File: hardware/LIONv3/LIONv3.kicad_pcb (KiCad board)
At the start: 4 copper layers, 45 x 80 mm, 77 parts, among them SW1 RESET, SW2 BOOT, U1 TCAN3414DR, U10 INA226AIDGSR, U11 TPS259474ARPWR, U12 XL-1608UGC-04, U13 XL-1608SURC-06, U14 UART, U15 I2C, U16 CAN, U17 PWR_3V3, U18 PWR_5V, U19 PWR_GND, U2 TYPE-C_16PIN_2MD(073), U20 TLV76733DRVR, U3 ESP32-C6-MINI-1-N4, U4 TMP112AIDRLR, U5 E80-900M2213S, U6 INA226AIDGSR, U7 XL-1608UBC-04, U8 W25Q16JVSSIQTR

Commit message: feat(hardware): add final components position
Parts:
- added H1: M2.5, MountingHole:MountingHole_2.5mm_Pad_Via, F.Cu at (2.77, 2.77)
- added H2: M2.5, MountingHole:MountingHole_2.5mm_Pad_Via, F.Cu at (2.77, 9.32)
- added H3: M2.5, MountingHole:MountingHole_2.5mm_Pad_Via, F.Cu at (2.77, 15.9)
- added H4: M2.5, MountingHole:MountingHole_2.5mm_Pad_Via, F.Cu at (2.77, 22.4)
- added U9: HC-1_25-2PWT, LIONv3-Footprints:CONN-SMD_2P-P1.25-HC-1.25-2PWT, B.Cu at (199.7, 75.2)
- C16, C17, C18, C19, C20, C21, C22, D3, D4, R17, R18, R19, R20, R21, R22, R23, R32, U10, U11, U20: moved to B.Cu
- U14: value UART -> HC-1_25-2PWT; footprint LIONv3-Footprints:CONN-SMD_4P-P1.25_53261-0471 -> LIONv3-Footprints:CONN-SMD_2P-P1.25-HC-1.25-2PWT
- U15: value I2C -> HC-1_25-2PWT; footprint LIONv3-Footprints:CONN-SMD_4P-P1.25_53261-0471 -> LIONv3-Footprints:CONN-SMD_2P-P1.25-HC-1.25-2PWT
- U16: value CAN -> HC-1_25-2PWT; footprint LIONv3-Footprints:CONN-SMD_4P-P1.25_53261-0471 -> LIONv3-Footprints:CONN-SMD_2P-P1.25-HC-1.25-2PWT
- U17: value PWR_3V3 -> HC-1_25-2PWT; footprint LIONv3-Footprints:CONN-SMD_4P-P1.25_53261-0471 -> LIONv3-Footprints:CONN-SMD_2P-P1.25-HC-1.25-2PWT
- U18: value PWR_5V -> HC-1_25-2PWT; footprint LIONv3-Footprints:CONN-SMD_4P-P1.25_53261-0471 -> LIONv3-Footprints:CONN-SMD_2P-P1.25-HC-1.25-2PWT
- U19: value PWR_GND -> HC-1_25-2PWT; footprint LIONv3-Footprints:CONN-SMD_4P-P1.25_53261-0471 -> LIONv3-Footprints:CONN-SMD_2P-P1.25-HC-1.25-2PWT
- moved U17 122.7 mm to (199.2, 84.6), turned to -90 degrees
- moved U16 114.2 mm to (199.2, 94.3), turned to -90 degrees
- moved U14 94.1 mm to (162.1, 85.5), turned to 90 degrees
- moved U15 88.1 mm to (162.1, 76.9), turned to 90 degrees
- moved R12 88.0 mm to (184.1, 95.3)
- moved U6 88.0 mm to (178.2, 96.1)
- moved C12 88.0 mm to (182.1, 96.8)
- moved D1 85.6 mm to (168.1, 85.5), turned to 0 degrees
- moved U18 83.9 mm to (162.1, 68.3), turned to 90 degrees
- moved R18 79.9 mm to (186.4, 70.8), turned to 180 degrees
- moved C16 79.6 mm to (184.9, 72.5), turned to 0 degrees
- moved JP1 77.9 mm to (170.4, 82.4), turned to 90 degrees
- moved R3 76.0 mm to (169.7, 88.4), turned to 90 degrees
- moved U10 74.4 mm to (185.7, 76.3), turned to 180 degrees
- moved R2 74.4 mm to (170.9, 88.4), turned to -90 degrees
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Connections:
- D1 pad 1: /CAN_A_P -> /CAN_A_N
- D1 pad 2: /CAN_A_N -> /CAN_A_P
- U14 pad 1: +3.3V -> /CAN_A_N
- U14 pad 2: /UART_TX0 -> /CAN_A_P
- U14 pad 3: /UART_RX0 -> GND
- U15 pad 1: /I2C_SDA -> /I2C_SCL
- U15 pad 2: unconnected-(U15-Pad2) -> /I2C_SDA
- U15 pad 3: unconnected-(U15-Pad3) -> GND
- U15 pad 4: /I2C_SCL -> GND
- U16 pad 1: unconnected-(U16-Pad1) -> /3V3_IN
- U16 pad 2: /CAN_A_P -> /3V3_IN
- U16 pad 3: /CAN_A_N -> GND
- U16 pad 4: unconnected-(U16-Pad4) -> GND
- U17 pad 1: /3V3_IN -> +5V
- U17 pad 2: /3V3_IN -> +5V
- U17 pad 3: /3V3_IN -> GND
- U17 pad 4: /3V3_IN -> GND
- U18 pad 1: +5V -> GND
- U18 pad 2: +5V -> GND
- U18 pad 3: +5V -> GND
- U18 pad 4: +5V -> GND
- U19 pad 1: GND -> /CAN_A_N
- U19 pad 2: GND -> /CAN_A_P
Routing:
- net +3.3V: vias 21 -> 1
- net GND: vias 20 -> 69
- net /POWER/PWR: vias 13 -> 2
- net /POWER/5V_D: vias 8 -> 2
- net /POWER/3V3_IN: vias 19 -> 0
- added copper zone on B.Cu, net /POWER/5V_D
- added copper zone on B.Cu, net /POWER/PWR
- added copper zone on B.Cu, net GND
- removed copper zone on F.Cu, net +3.3V
- removed copper zone on F.Cu, net /POWER/3V3_IN
- removed copper zone on F.Cu, net /POWER/5V_D
- removed copper zone on F.Cu, net /POWER/PWR
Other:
- board size 45 x 80 mm -> 45 x 85.1 mm

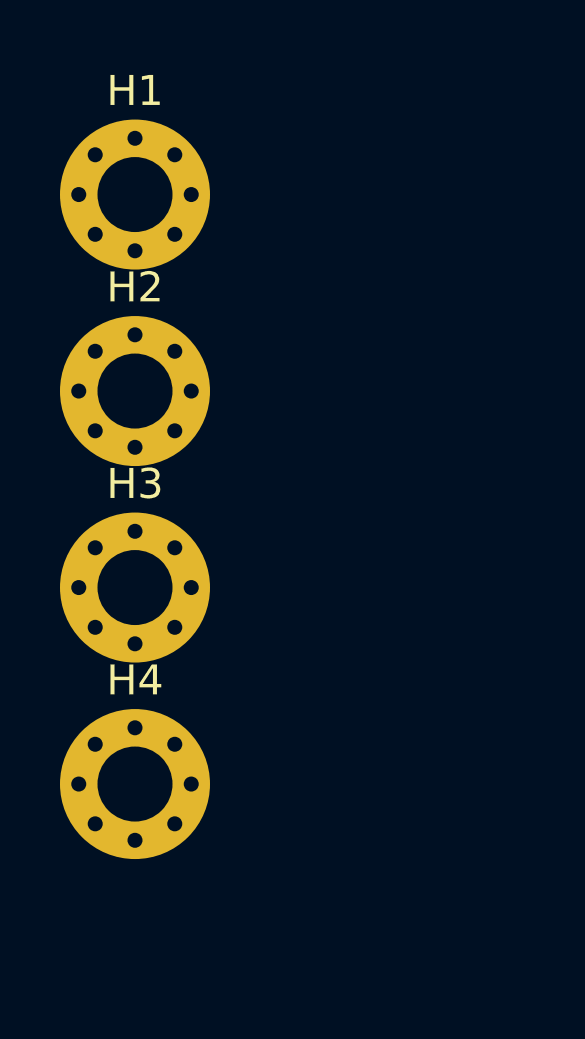
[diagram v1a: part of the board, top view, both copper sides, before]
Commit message: feat(hardware): organize repo structure
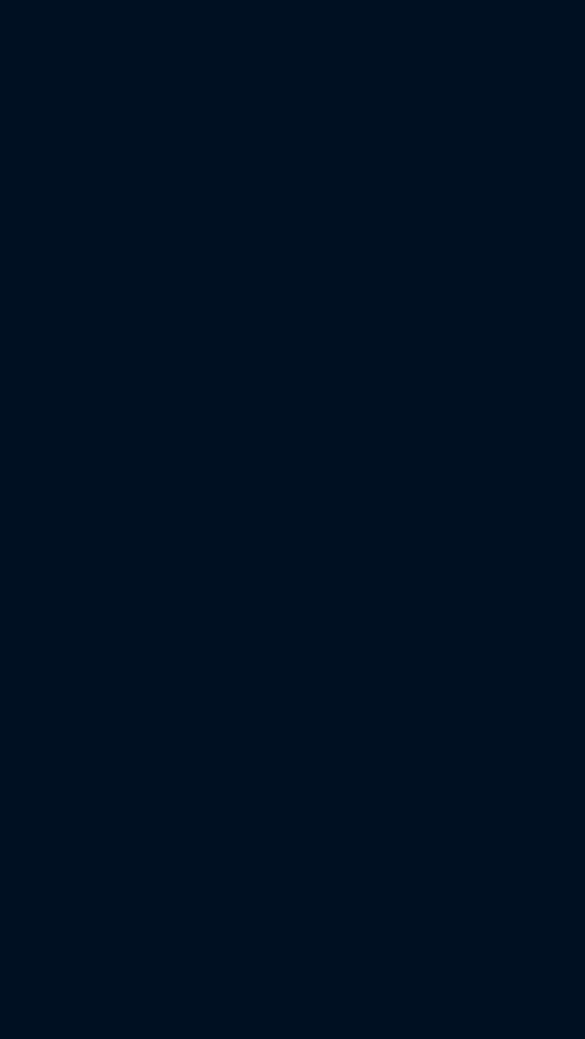
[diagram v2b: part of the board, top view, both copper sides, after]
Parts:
- removed H1, H2, H3, H4: M2.5, MountingHole:MountingHole_2.5mm_Pad_Via

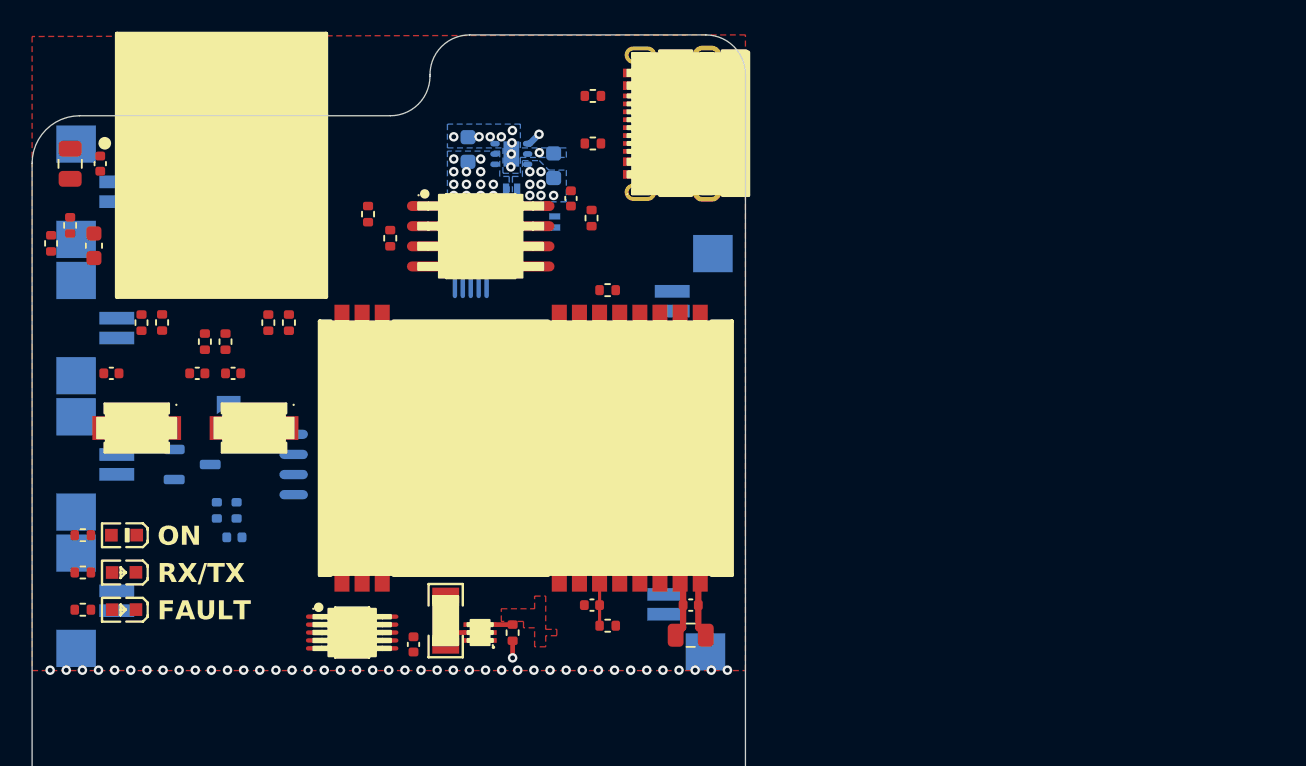
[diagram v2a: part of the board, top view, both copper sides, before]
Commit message: feat(hardware): add power layout
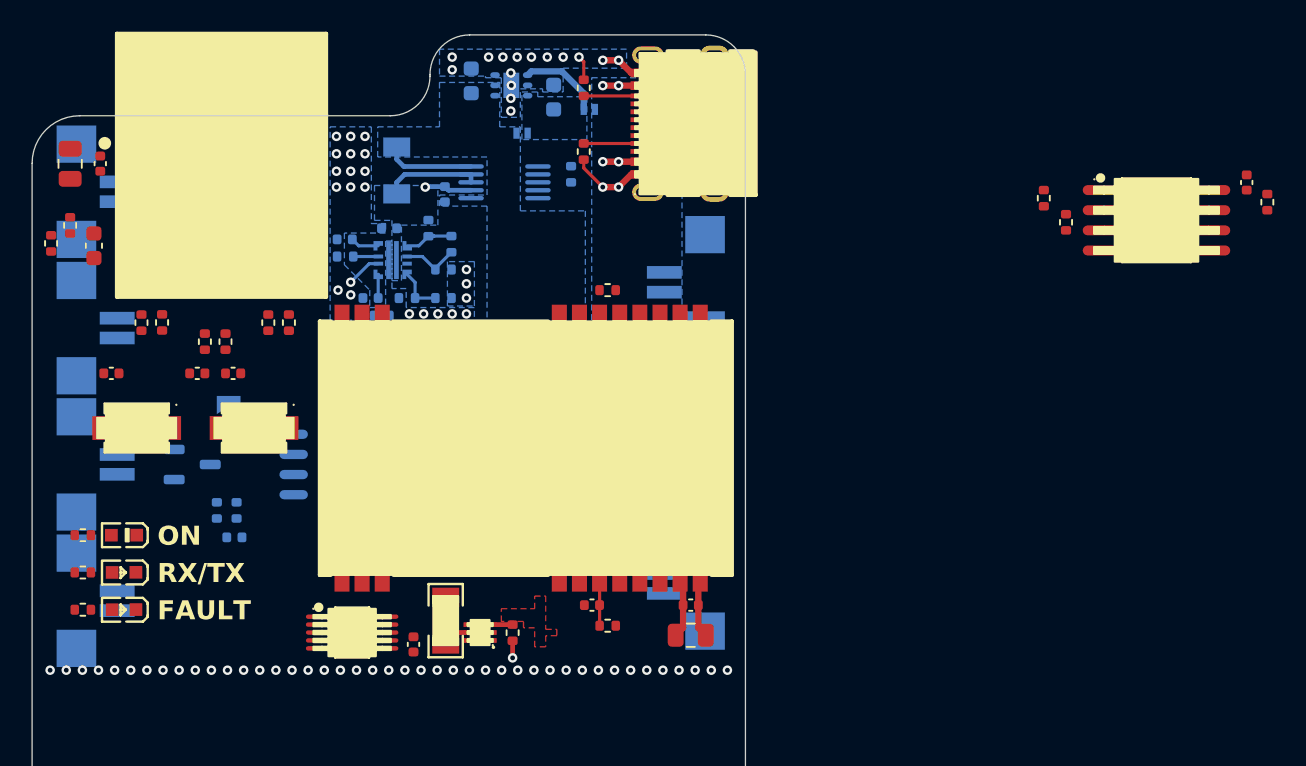
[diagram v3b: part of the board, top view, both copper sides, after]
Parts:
- moved C13 42.6 mm to (234.6, 67.7)
- moved R13 42.6 mm to (221.8, 68.7)
- moved R16 42.6 mm to (223.2, 70.2)
- moved U8 42.6 mm to (228.9, 70.1)
- moved R15 42.6 mm to (235.9, 68.9)
- moved U9 17.8 mm to (199.2, 93.0)
- moved R19 16.9 mm to (183.0, 70.6)
- moved R20 16.7 mm to (184.4, 71.6)
- moved C20 16.7 mm to (180.1, 76.1)
- moved R21 16.7 mm to (177.8, 72.4)
- moved R23 16.7 mm to (183.9, 75.0)
- moved R32 16.7 mm to (183.9, 73.2)
- moved C18 16.7 mm to (177.7, 71.3)
- moved C19 16.7 mm to (179.3, 75.0)
- moved R22 16.7 mm to (181.7, 75.0)
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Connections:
- U16 pad 1: /3V3_IN -> /POWER/PWR
- U16 pad 2: /3V3_IN -> /POWER/PWR
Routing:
- net GND: track 6.22 -> 24.3 mm, vias 69 -> 82
- net /POWER/3V3_IN: track 0.00 -> 6.13 mm
- net /POWER/PWR: track 0.00 -> 5.66 mm, vias 2 -> 0
- net +5V: track 0.00 -> 4.60 mm, vias 0 -> 4
- net /POWER/5V_D: track 0.97 -> 5.22 mm, vias 2 -> 0
- net Net-(U2-CC2): track 0.00 -> 3.50 mm
- net Net-(U2-CC1): track 0.00 -> 3.50 mm
- net +3.3V: vias 1 -> 11
- added copper zone on B.Cu, net +3.3V
- added copper zone on In2.Cu, net +3.3V
- added copper zone on B.Cu, net +5V
- added copper zone on B.Cu, net /POWER/3V3_IN
- added copper zone on In1.Cu, net GND

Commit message: feat(hardware): add RF circuit
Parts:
- removed U19: HC-1_25-2PWT, LIONv3-Footprints:CONN-SMD_2P-P1.25-HC-1.25-2PWT
- C12, R12, U6: moved to B.Cu
- moved R15 18.5 mm to (218.2, 63.9), turned to 0 degrees
- moved C13 17.9 mm to (216.9, 65.2), turned to 180 degrees
- moved R12 14.9 mm to (176.8, 82.3)
- moved U6 13.8 mm to (182.7, 83.1)
- moved C12 13.4 mm to (178.8, 83.8)
- moved U18 12.4 mm to (150.0, 65.4)
- moved R13 10.1 mm to (217.9, 78.0), turned to 180 degrees
- moved U8 9.66 mm to (219.3, 70.9), turned to 0 degrees
- moved R16 7.43 mm to (219.4, 76.6), turned to 0 degrees
- moved C1 7.00 mm to (183.4, 92.5)
- moved C2 7.00 mm to (181.6, 92.5)
- moved C6 7.00 mm to (170.8, 97.1)
- moved D1 7.00 mm to (168.1, 92.5)
- moved JP1 7.00 mm to (170.4, 89.4)
- moved R2 7.00 mm to (170.9, 95.4)
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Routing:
- net Net-(C3-Pad1): track 0.00 -> 12.6 mm
- net GND: track 24.3 -> 36.8 mm, vias 82 -> 124
- net +3.3V: track 2.28 -> 14.7 mm, vias 11 -> 15
- net /IO9: track 0.00 -> 9.00 mm, vias 0 -> 2
- net /I2C_SDA: track 0.00 -> 7.00 mm, vias 0 -> 1
- net /I2C_SCL: track 0.00 -> 6.96 mm, vias 0 -> 1
- net Net-(U3-EN): track 0.00 -> 4.85 mm
- net 3.3V_RF: track 4.07 -> 8.36 mm, vias 0 -> 2
- net /LR_NSS: track 0.00 -> 3.48 mm, vias 0 -> 1
- net /IO8: track 0.00 -> 1.80 mm
- net /TMP_ALERT: track 1.30 -> 2.36 mm, vias 0 -> 1
- net /LR_RST: track 3.20 -> 4.00 mm

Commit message: feat(hardware): change SPI terminology (new OSHWA naming conventions)
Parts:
- removed C3: 100nF, Capacitor_SMD:C_0402_1005Metric
- removed R1: 0, Resistor_SMD:R_0402_1005Metric
- added C23: 100nF, Capacitor_SMD:C_0402_1005Metric, F.Cu at (245.4, 100.3)
- added D2: ESD9B3.3ST5G, Diode_SMD:D_SOD-923, F.Cu at (252.8, 102.7)
- added D5: ESD9B3.3ST5G, Diode_SMD:D_SOD-923, F.Cu at (248.2, 105.9)
- added D6: D_Schottky, LIONv3-Footprints:X2-DFN1006-2_L1.0-W0.6-P0.65-RD, F.Cu at (251.6, 92.8)
- added FB1: 220Ω@100MHz, Capacitor_SMD:C_0805_2012Metric, F.Cu at (259.2, 105.5)
- added FB2: 220Ω@100MHz, Capacitor_SMD:C_0805_2012Metric, F.Cu at (239.1, 108.3)
- added U19: HC-1_25-2PWT, LIONv3-Footprints:CONN-SMD_2P-P1.25-HC-1.25-2PWT, F.Cu at (235.0, 93.6)
- added U21: USBLC6-2SC6, Package_TO_SOT_SMD:SOT-23-6, F.Cu at (226.9, 100.5)
- R14: value 68 -> 1k
- R24: value 82 -> 2.2k
- R25: value 150 -> 1k
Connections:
- C21 pad 1: /POWER/5V_D -> +5V
- C4 pad 1: Net-(U3-EN) -> Net-(D2-A2)
- D3 pad 1: /POWER/5V_D -> +5V
- D3 pad 2: +5V -> Net-(D3-A)
- D4 pad 1: /POWER/5V_D -> +5V
- R4 pad 2: Net-(U3-EN) -> Net-(D2-A2)
- SW1 pad 2: Net-(C3-Pad1) -> Net-(D2-A2)
- U17 pad 1: +5V -> Net-(FB2-Pad2)
- U17 pad 2: +5V -> Net-(FB2-Pad2)
- U2 pad A4B9: +5V -> Net-(FB1-Pad2)
- U2 pad A6: /USB_D+ -> /D+
- U2 pad A7: /USB_D- -> /D-
- U2 pad B4A9: +5V -> Net-(FB1-Pad2)
- U2 pad B6: /USB_D+ -> /D+
- U2 pad B7: /USB_D- -> /D-
- U20 pad 4: /POWER/5V_D -> +5V
- U20 pad 6: /POWER/5V_D -> +5V
- U3 pad 8: Net-(U3-EN) -> Net-(D2-A2)
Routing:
- net Net-(D2-A2): track 0.00 -> 17.4 mm
- net Net-(C3-Pad1): track 12.6 -> 0.00 mm
- net /POWER/5V_D: track 5.22 -> 0.00 mm
- net Net-(U3-EN): track 4.85 -> 0.00 mm
- net Net-(FB1-Pad2): track 0.00 -> 4.60 mm, vias 0 -> 4
- net +5V: track 4.60 -> 5.22 mm, vias 4 -> 0
- removed copper zone on B.Cu, net /POWER/5V_D
